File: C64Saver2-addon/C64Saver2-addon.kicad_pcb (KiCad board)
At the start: 2 copper layers, 43.9 x 29 mm, 39 parts, among them CON1 AVR-ISP-6, J1 Conn_01x08_Female, J2 Conn_01x08_Female, J3 OLED_128x32_Conn_01x04_Male, J4 Conn_01x04_Female, SW1 SW_Push, U1 INA219xIDR-SOIC, U2 ISO1541D, U3 ATTINY85-20SU, U4 TLP291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

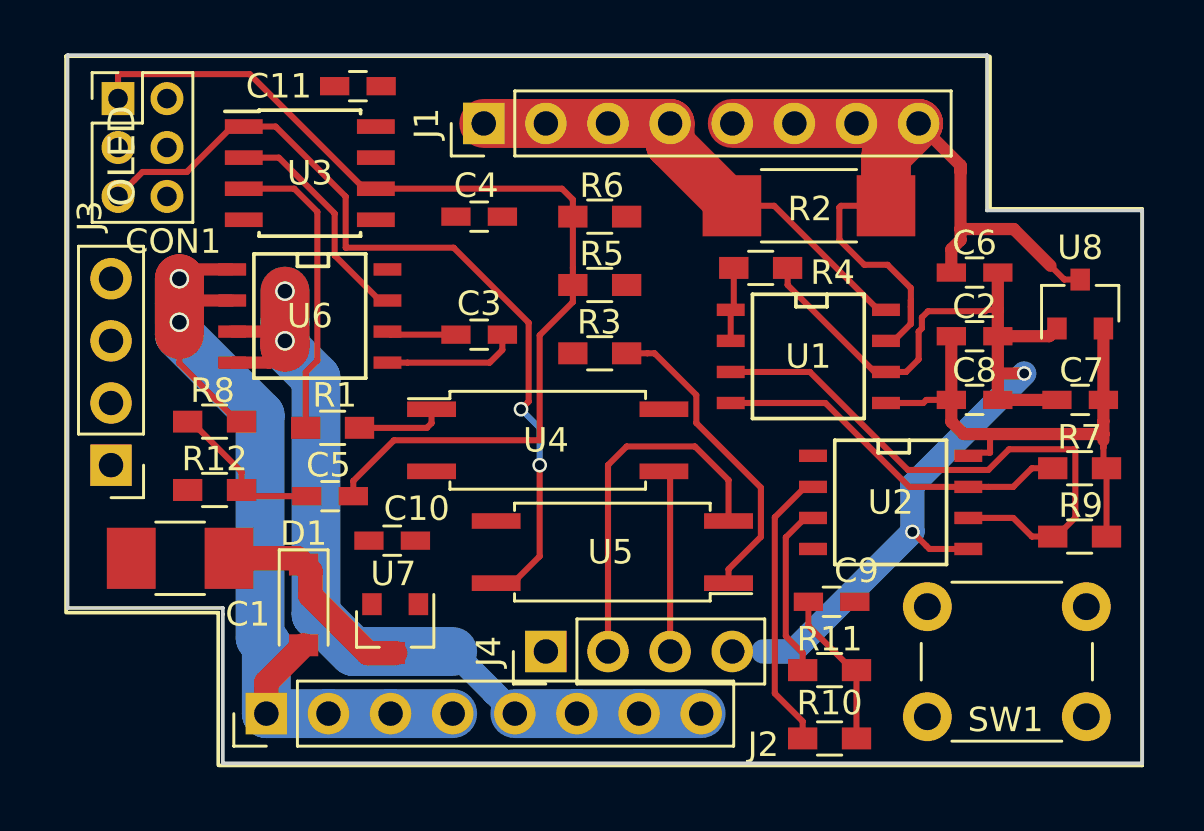
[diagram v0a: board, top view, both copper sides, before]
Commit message: more routing. mostly power nets remaining
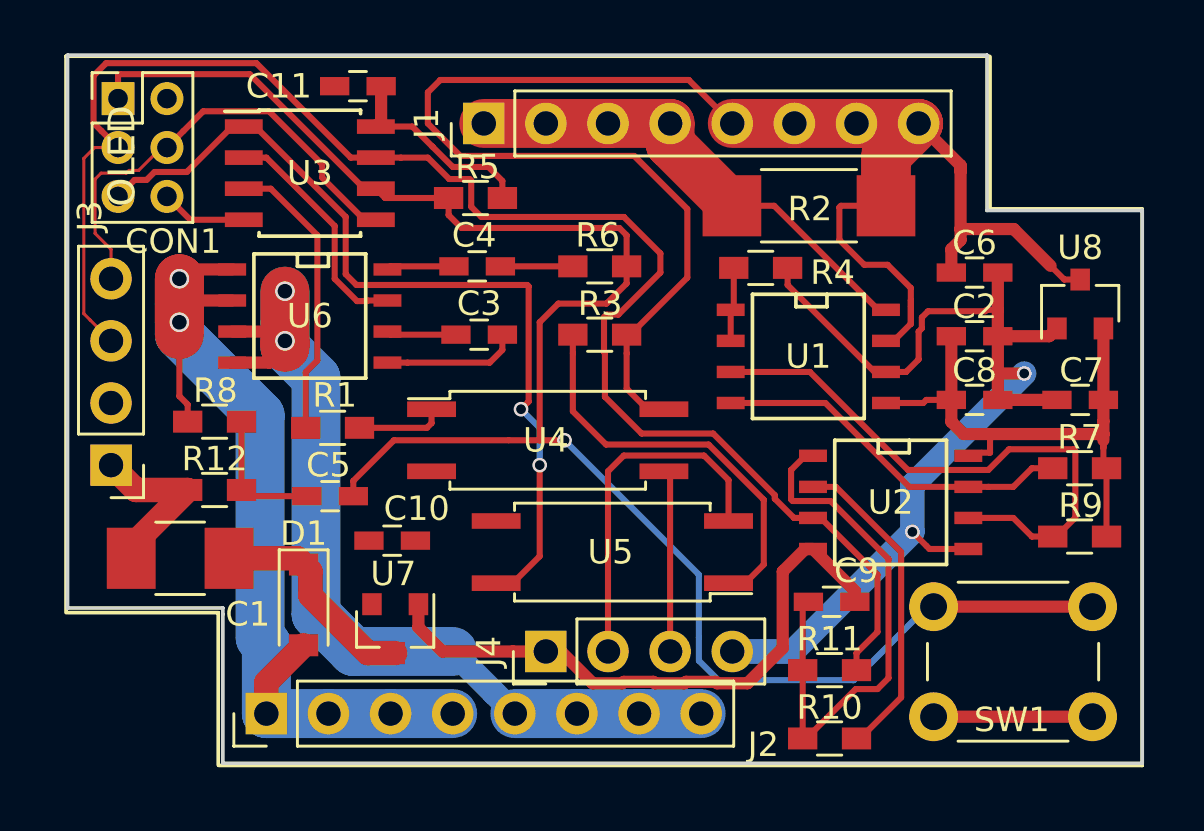
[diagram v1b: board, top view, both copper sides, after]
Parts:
- moved R5 6.20 mm to (157.1, 89.4)
- moved C4 2.03 mm to (157.2, 92.2)
- moved R6 2.03 mm to (162.2, 92.2), turned to 0 degrees
- moved R3 0.76 mm to (162.2, 95.0), turned to 0 degrees
- moved SW1 0.25 mm to (182.4, 110.6)
- turned R10 to 180 degrees
- turned R11 to 180 degrees
- turned R8 to 180 degrees
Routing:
- net /SCL1: track 7.16 -> 65.4 mm
- net GND: track 5.54 -> 50.9 mm
- net VIN-: track 40.3 -> 77.3 mm
- net /SENSE_VAC: track 41.0 -> 74.6 mm, vias 0 -> 1
- net +5V: track 6.60 -> 33.8 mm
- net /SDA1: track 11.6 -> 32.4 mm
- net Net-(R3-Pad1): track 12.9 -> 16.8 mm
- net GNDD: track 43.5 -> 44.8 mm
- net /#OVERVOLTAGE: track 34.7 -> 35.8 mm
- net Net-(C5-Pad1): track 6.57 -> 5.57 mm
- net /9VAC1+: track 44.4 -> 43.4 mm
- net /HOLD_: track 12.4 -> 11.9 mm
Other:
- rule trace_min: 0.2 -> 0.127

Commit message: routing completed
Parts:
- moved C11 0.25 mm to (152.1, 84.8), turned to 180 degrees
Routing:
- net +5V: track 33.8 -> 102.7 mm, vias 0 -> 5
- net /SDA1: track 32.4 -> 61.7 mm, vias 0 -> 2
- net GNDD: track 44.8 -> 47.2 mm
- net GND: track 50.9 -> 52.7 mm, vias 0 -> 4
- net /9VAC1+: track 43.4 -> 41.6 mm
- net /SENSE_VAC: track 74.6 -> 76.1 mm, vias 1 -> 2
- net /SCL1: track 65.4 -> 66.5 mm
- net VIN-: track 77.3 -> 76.2 mm
- net /#OVERVOLTAGE: track 35.8 -> 35.0 mm
- added copper zone on B.Cu, net GND
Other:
- board text added: "C64 Saver Addon Rev 1.0 BWACK 2018"
- board text removed: "C64 Saver Addon BWACK 2018"
